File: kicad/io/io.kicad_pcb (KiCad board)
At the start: 2 copper layers, 160 x 100.3 mm, 49 parts, among them IC1 ATMEGA8-P, P1 PS/2 Keyboard, P2 SDCARD, P3 ISP, P4 SPI4, P5 CONN_02X25, P6 SPI5, P7 SPI6, U1 G65SC22P, U2 7407, U3 7400, U4 74125, U5 LP2950, U6 LTV846, U7 DS1306, U8 LTV846, X1 CRYSTAL_SMD

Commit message: cleanup
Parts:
- removed P2: SDCARD, Sockets:SDCARD-REVERSE
- added SDCARD1: SD_Card, Connect:SD_Card_Receptacle, F.Cu at (92.7, 119.4)
- moved C5 29.2 mm to (96.5, 133.3), turned to 270 degrees
- moved U2 14.0 mm to (109.2, 135.9), turned to 0 degrees
- moved R4 12.7 mm to (82.5, 100.3)
- moved R7 8.16 mm to (162.6, 85.1), turned to 90 degrees
- moved R3 7.62 mm to (85.1, 100.3)
- moved R5 7.62 mm to (92.7, 100.3)
- moved C10 5.08 mm to (96.5, 119.4), turned to 270 degrees
- moved R11 4.02 mm to (157.5, 85.1)
- moved R12 4.02 mm to (154.9, 85.1)
- moved R10 4.02 mm to (149.9, 85.1)
- moved R8 4.02 mm to (160.0, 85.1)
- moved R9 4.02 mm to (152.4, 85.1)
- moved R1 2.54 mm to (90.2, 100.3)
- moved R2 2.54 mm to (87.6, 100.3)
- moved C2 1.27 mm to (68.6, 101.6)
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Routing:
- net GND: track 426.6 -> 397.1 mm
- net Net-(R5-Pad2): track 31.3 -> 6.43 mm
- net /SD Card/SPI_SS1: track 99.6 -> 121.8 mm
- net Net-(R4-Pad2): track 7.51 -> 29.0 mm
- net Net-(C10-Pad1): track 66.2 -> 47.1 mm
- net /Joystick Ports/J_Fire2: track 21.2 -> 34.2 mm
- net Net-(R3-Pad2): track 32.5 -> 42.0 mm
- net VCC: track 412.1 -> 402.6 mm
- net Net-(SDCARD1-Pad7): track 92.2 -> 83.5 mm, vias 2 -> 0
- net Net-(R2-Pad2): track 38.4 -> 45.0 mm
- net /SD Card/SPI_MOSI: track 164.0 -> 168.5 mm
- net /NMI: track 118.1 -> 113.9 mm
- net Net-(U3-Pad8): track 66.1 -> 70.2 mm
- net /Joystick Ports/J_Right: track 75.3 -> 79.1 mm
- net /Joystick Ports/J_Down: track 33.2 -> 36.8 mm
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
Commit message: fixes, pinleiste via port a
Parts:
- added P2: CONN_02X06, Pin_Headers:Pin_Header_Straight_2x06, F.Cu at (156.2, 76.2)
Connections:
- net VCC renamed Vcc
- U1 pad 39: (no net) -> /CA2
- U1 pad 40: (no net) -> /CA1
- U1 pad 7: (no net) -> /Joystick Ports/J_Fire2
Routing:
- net GND: track 397.1 -> 467.0 mm
- net /CA1: track 0.00 -> 31.5 mm
- net /CA2: track 0.00 -> 27.9 mm
- net Vcc: track 402.6 -> 428.7 mm
- net /Joystick Ports/J_Fire2: track 34.2 -> 50.4 mm
- net /RESET: track 165.2 -> 151.1 mm, vias 0 -> 1
- net /Joystick Ports/PortSel01: track 31.4 -> 40.4 mm
- net /NMI: track 113.9 -> 107.6 mm
- net /Joystick Ports/J_Fire1: track 49.0 -> 44.4 mm, vias 1 -> 2
- net /Joystick Ports/J_Up: track 31.8 -> 35.8 mm
- net Net-(SDCARD1-Pad7): track 83.5 -> 81.0 mm
- net /Joystick Ports/PortSel02: track 26.5 -> 28.8 mm
- net /Joystick Ports/J_Right: track 79.1 -> 77.1 mm
- net /Joystick Ports/J_Down: track 36.8 -> 38.7 mm
- net /Connector/RESET_TRIG: track 127.0 -> 128.5 mm
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
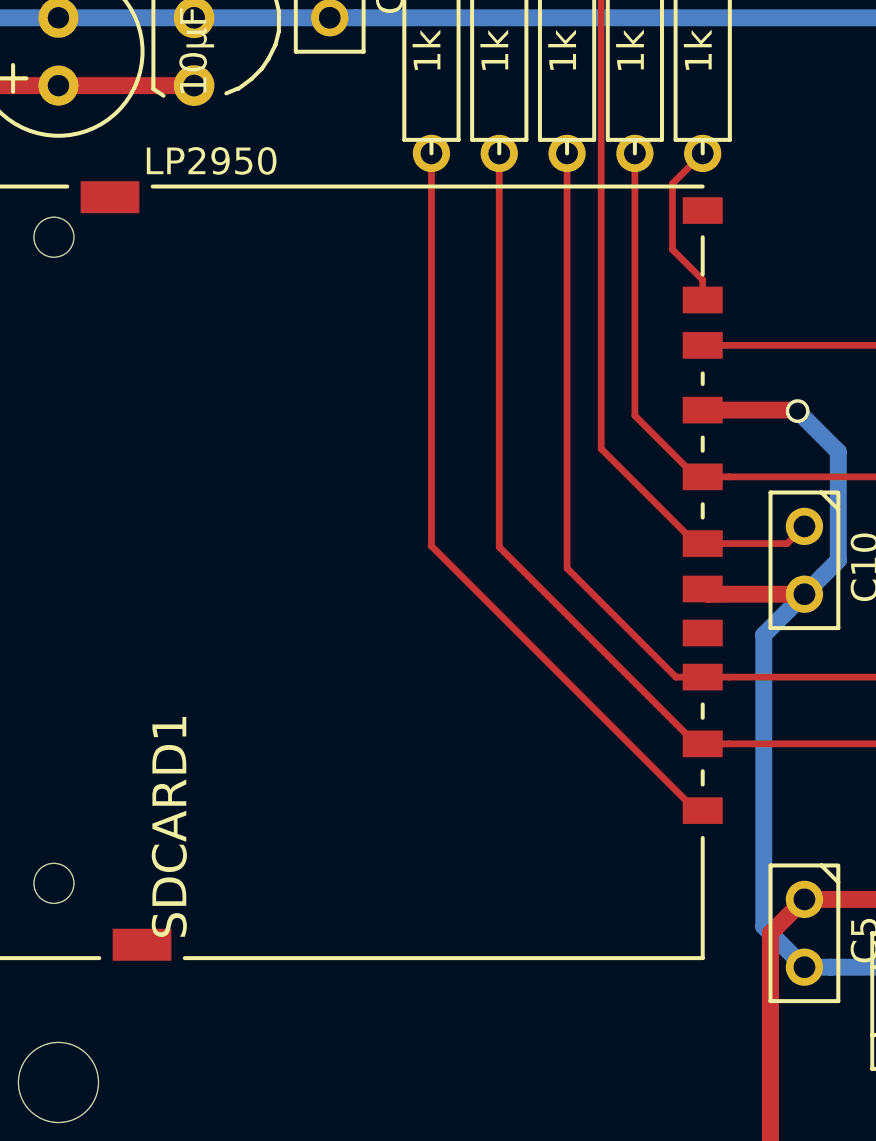
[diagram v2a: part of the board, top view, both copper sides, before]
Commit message: kupferflaechen f sd sockel
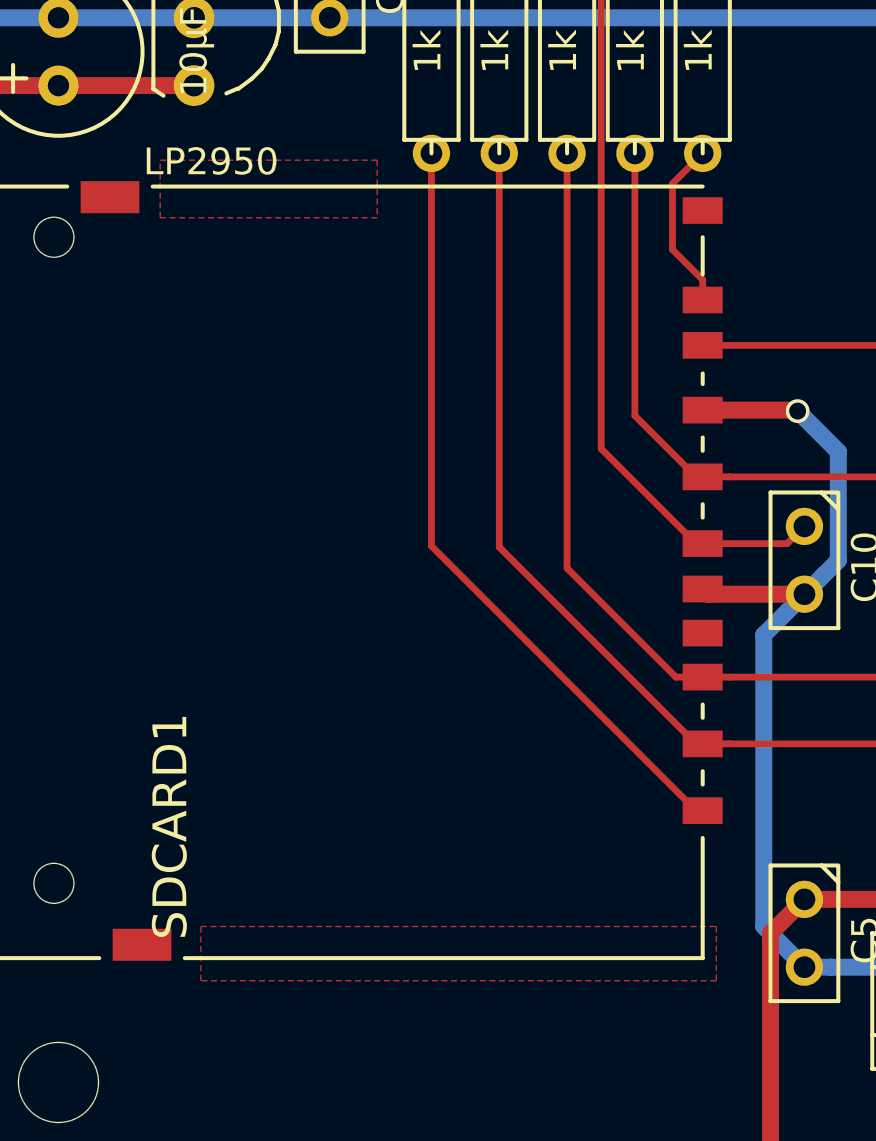
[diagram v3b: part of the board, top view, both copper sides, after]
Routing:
- added copper zone on F.Cu, net (none)

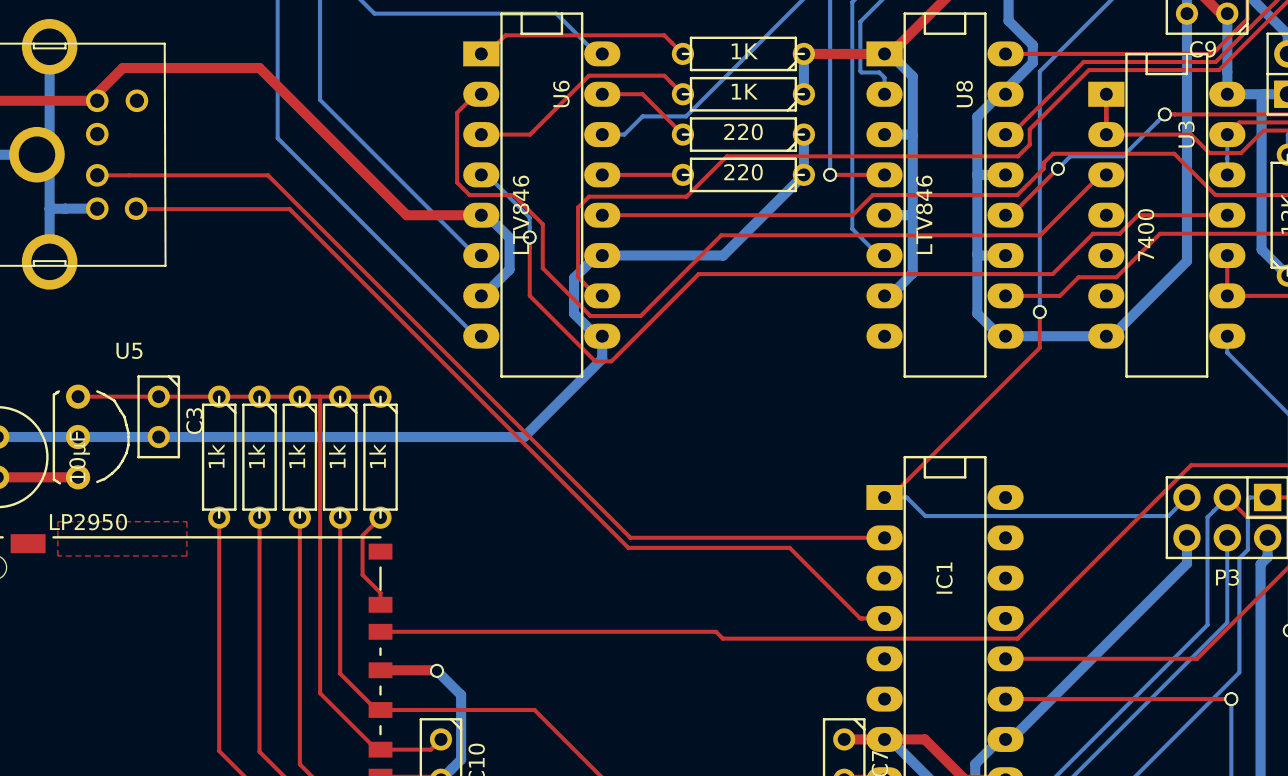
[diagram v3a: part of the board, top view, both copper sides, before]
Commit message: vorbereitung ps2 maus
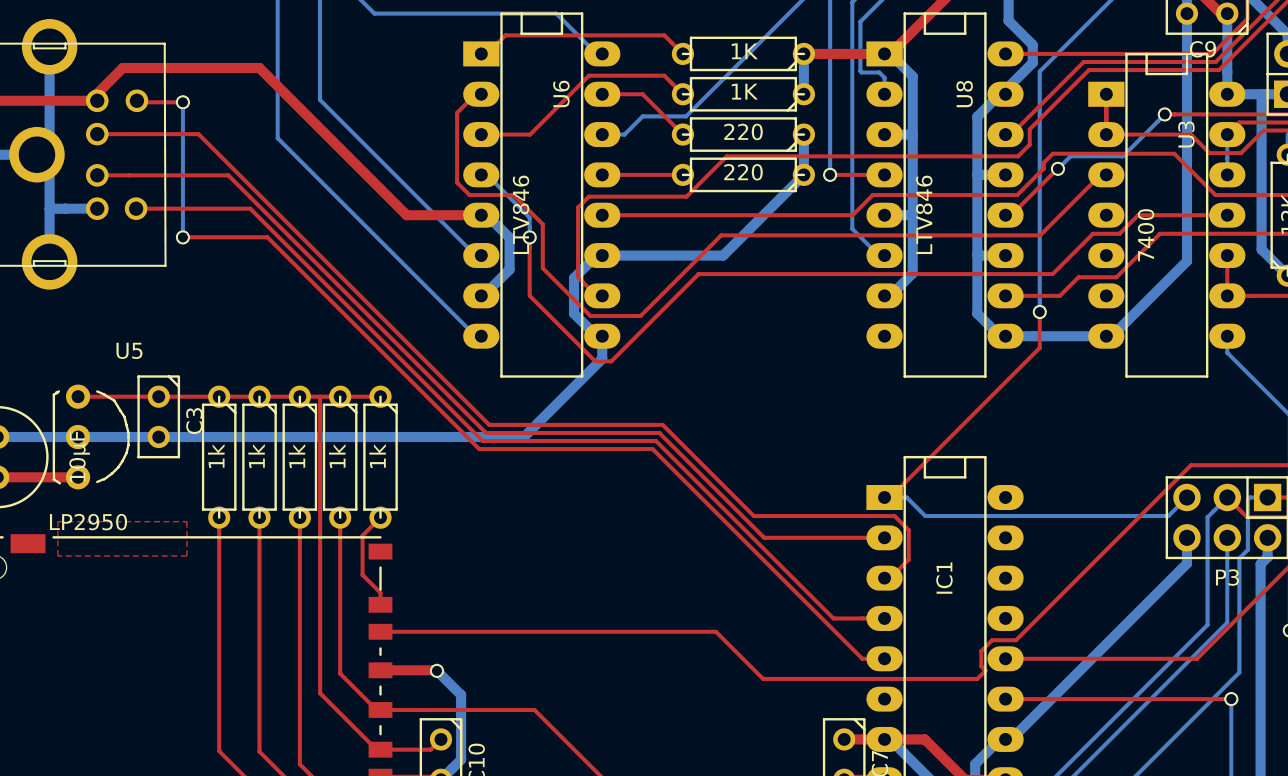
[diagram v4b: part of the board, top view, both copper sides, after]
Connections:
- net Vcc renamed VCC
- IC1 pad 3: (no net) -> Net-(IC1-Pad3)
- IC1 pad 5: (no net) -> Net-(IC1-Pad5)
- P1 pad 2: (no net) -> Net-(IC1-Pad3)
- P1 pad 8: (no net) -> Net-(IC1-Pad5)
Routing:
- net Net-(IC1-Pad5): track 0.00 -> 66.6 mm, vias 0 -> 2
- net Net-(IC1-Pad3): track 0.00 -> 65.3 mm
- net Net-(SDCARD1-Pad7): track 81.0 -> 84.2 mm

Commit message: andere db9
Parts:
- Port1, Port2: footprint Connect:DB9MC -> Connectors:DB_9M
- moved Port1 9.80 mm to (89.5, 56.3), turned to 180 degrees
- moved Port2 9.80 mm to (122.6, 56.3), turned to 180 degrees
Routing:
- net GND: track 467.0 -> 437.5 mm
- net VCC: track 428.7 -> 420.0 mm
- net Net-(Port2-Pad8): track 23.5 -> 32.1 mm, vias 0 -> 1
- net Net-(Port1-Pad9): track 46.0 -> 52.4 mm, vias 1 -> 2
- net Net-(Port1-Pad3): track 59.2 -> 64.8 mm, vias 1 -> 2
- net Net-(Port1-Pad4): track 66.3 -> 70.3 mm, vias 0 -> 2
- net Net-(Port1-Pad5): track 34.8 -> 38.8 mm, vias 0 -> 2
- net Net-(Port1-Pad6): track 62.6 -> 66.5 mm, vias 0 -> 2
- net Net-(Port1-Pad7): track 37.1 -> 39.3 mm, vias 0 -> 2
- net Net-(Port1-Pad8): track 25.4 -> 27.4 mm
- net Net-(Port1-Pad2): track 58.1 -> 58.6 mm, vias 1 -> 2
- net Net-(Port1-Pad1): track 54.0 -> 54.4 mm, vias 1 -> 2

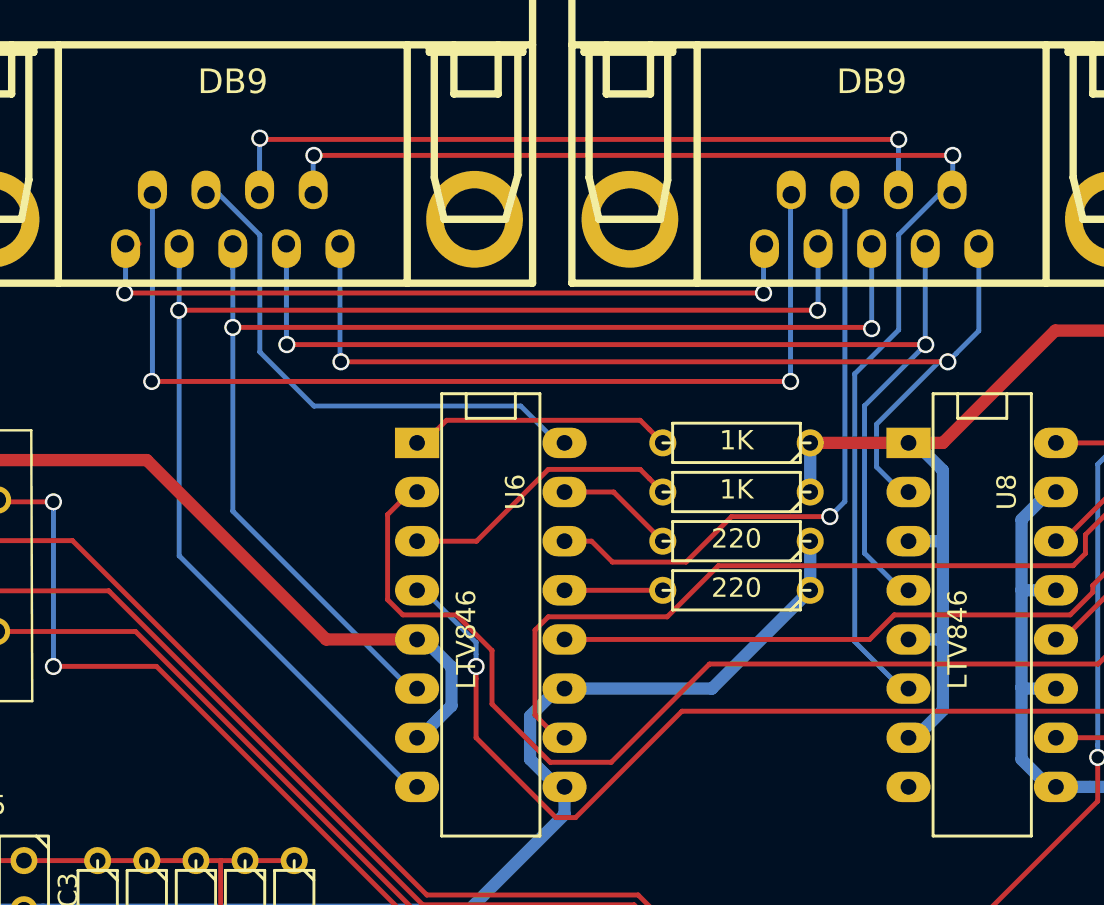
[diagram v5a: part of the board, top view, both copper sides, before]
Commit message: layout joyports
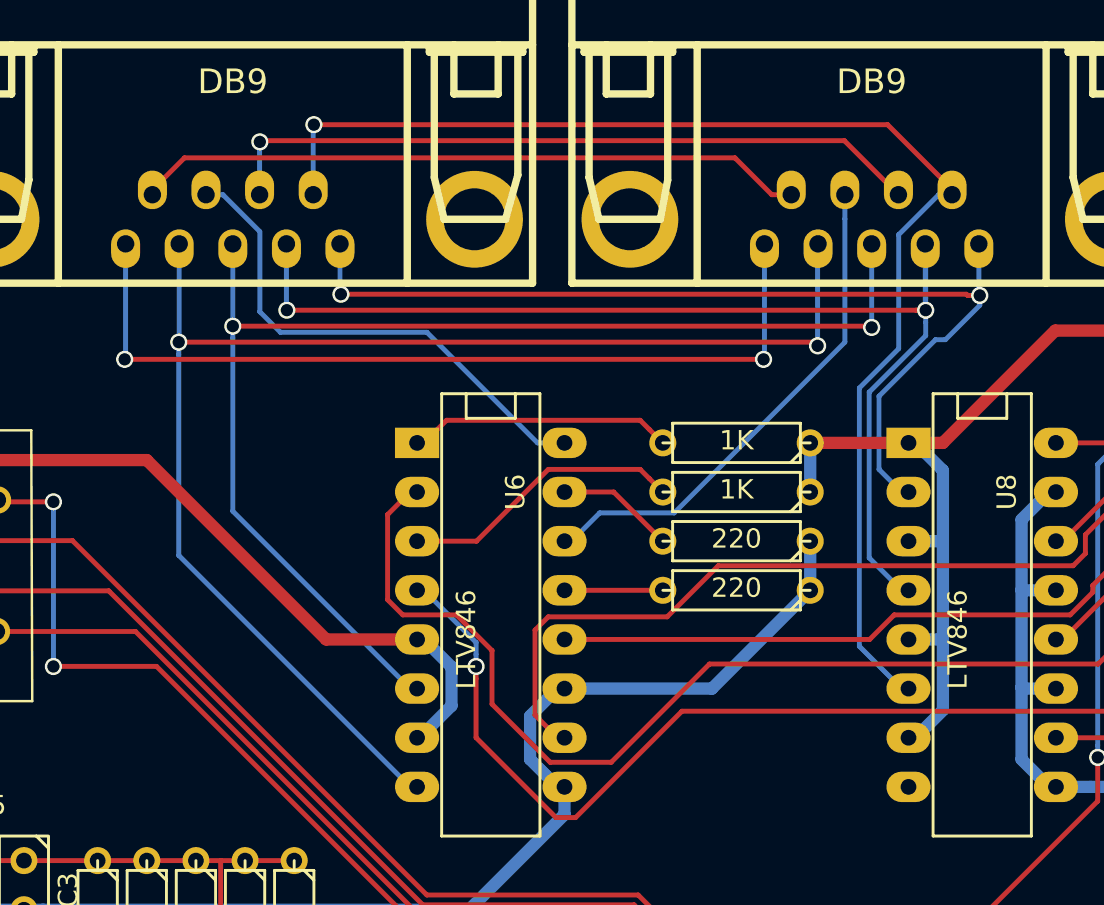
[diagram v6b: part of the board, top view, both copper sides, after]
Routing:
- net Net-(Port1-Pad9): track 52.4 -> 34.8 mm, vias 2 -> 0
- net Net-(Port1-Pad5): track 38.8 -> 45.1 mm
- net Net-(Port2-Pad8): track 32.1 -> 26.4 mm, vias 1 -> 0
- net Net-(Port1-Pad2): track 58.6 -> 60.5 mm
- net Net-(Port1-Pad4): track 70.3 -> 72.3 mm
- net Net-(Port1-Pad7): track 39.3 -> 37.4 mm, vias 2 -> 1
- net Net-(Port1-Pad1): track 54.4 -> 52.5 mm
- net Net-(Port1-Pad6): track 66.5 -> 67.5 mm, vias 2 -> 1
- net Net-(Port1-Pad8): track 27.4 -> 26.6 mm

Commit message: 3d models
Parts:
- SDCARD1: footprint Connect:SD_Card_Receptacle -> Conn_misc:sd_socket
- moved SDCARD1 14.6 mm to (78.1, 119.8)
- moved R1 2.88 mm to (88.3, 98.2)
- moved R2 2.88 mm to (85.7, 98.2)
- moved R3 2.88 mm to (83.2, 98.2)
- moved R4 2.88 mm to (80.6, 98.2)
- moved R5 2.88 mm to (90.8, 98.2)
- moved C3 2.25 mm to (78.1, 95.6)
- moved U5 2.25 mm to (73.0, 96.9)
- moved C2 2.25 mm to (67.9, 99.4)
- moved C10 2.16 mm to (94.6, 120.4)
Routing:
- net GND: track 437.5 -> 446.4 mm
- net Net-(C10-Pad1): track 47.1 -> 50.5 mm
- net Net-(R4-Pad2): track 29.0 -> 32.2 mm
- net Net-(R3-Pad2): track 42.0 -> 45.2 mm
- net Net-(R2-Pad2): track 45.0 -> 47.7 mm
- net Net-(R1-Pad2): track 44.8 -> 47.4 mm
- net Net-(R5-Pad2): track 6.43 -> 8.84 mm
- removed copper zone on F.Cu, net (none)

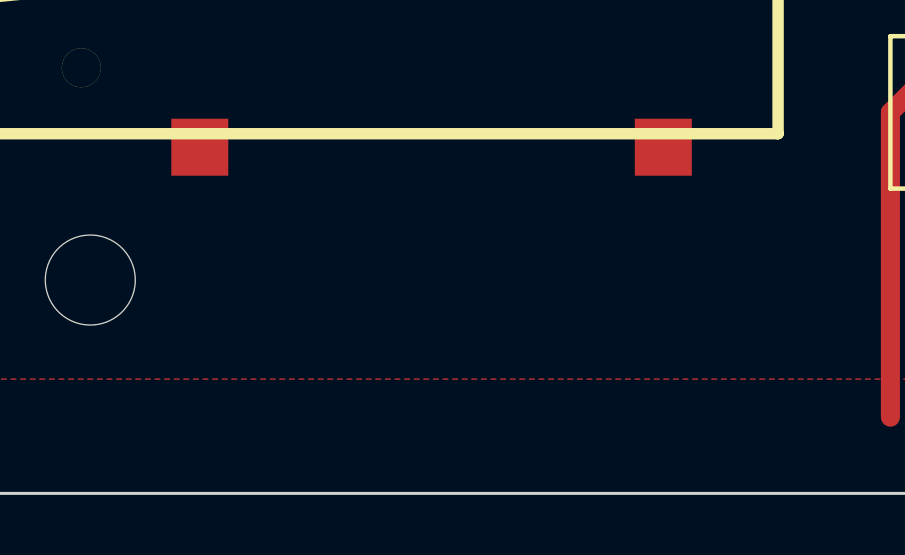
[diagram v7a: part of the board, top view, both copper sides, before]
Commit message: 3d models, layer label
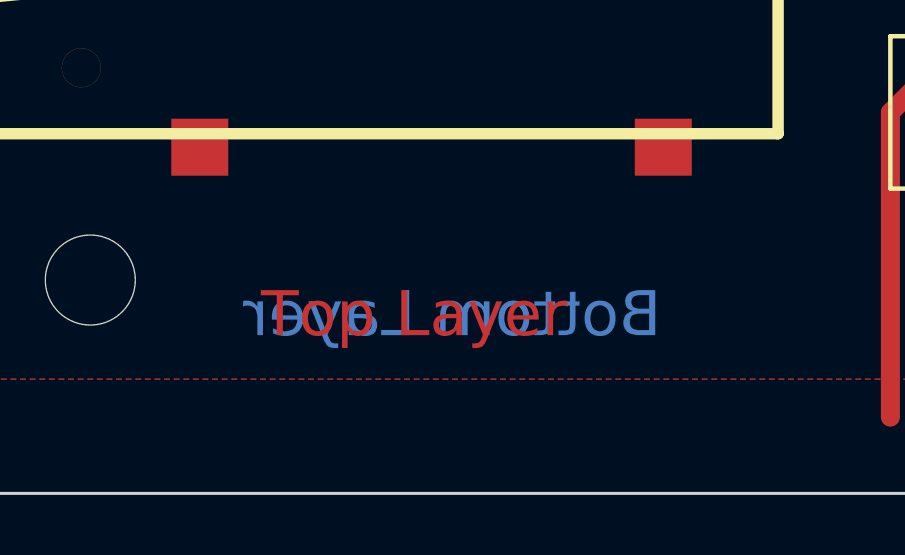
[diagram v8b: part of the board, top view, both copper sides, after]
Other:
- board text added: "Bottom Layer"
- board text added: "Top Layer"
